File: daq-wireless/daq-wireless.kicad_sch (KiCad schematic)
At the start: 2 parts

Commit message: Easter eggs
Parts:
- added J3: USB_C_Receptacle_USB2.0, symbol Connector:USB_C_Receptacle_USB2.0
- added J4: 5223002-2, !footprints:52230042, symbol semiactive-altium-import:0_mirrored_5223002-2
- added R2, R3: 5.1k, symbol Device:R
- J2: renamed from J?; footprint (none) -> Connector_Card:microSD_HC_Hirose_DM3AT-SF-PEJM5
- gave numbers to parts that had none: 1
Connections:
- new net: J3.A1 (GND), J3.A12 (GND), J3.B1 (GND), J3.B12 (GND)
- new net: J3.A4 (VBUS), J3.A9 (VBUS), J3.B4 (VBUS), J3.B9 (VBUS)
- new net: J3.A5 (CC1), R3.1
- new net: J3.B5 (CC2), R2.1
- new net 3.3V: J4.7, J4.8, J4.9
- new net 5V: J4.4, J4.5, J4.6
- new net 8.4V: J4.1, J4.2, J4.3
- new net CAN_H: J4.20
- new net CAN_L: J4.21
- new net CIPO: J4.17
- new net COPI: J4.18
- new net DIG_OUT: J4.24
- new net DIR1: J4.45
- new net DIR2: J4.46
- new net ENGHALL1: J4.26
- new net ENGHALL2: J4.38
- new net FRBPRESS: J4.47
- new net GND: J4.10, J4.11, J4.12, R2.2, R3.2
- new net I2C_CLK: J4.14
- new net I2C_DATA: J4.13
- new net IR_AMP: J4.35
- new net IR_TEENSY: J4.36
- new net N_A: J4.37
- new net PENC_A: J4.49
- new net PENC_B: J4.51
- new net PLDCLK: J4.57
- new net PLDDAT: J4.58
- new net PLOADC1: J4.41
- new net PLOADC2: J4.42
- new net PWM1: J4.43
- new net PWM2: J4.44
- new net RPOT1: J4.22
- new net RPOT2: J4.23
- new net RRBPRESS: J4.48
- new net RRHALL: J4.25
- new net RX: J4.16
- new net SCLK: J4.19
- new net SENC_A: J4.53
- new net SENC_B: J4.55
- new net SLDCLK: J4.59
- new net SLDDAT: J4.60
- new net SLOADC1: J4.39
- new net SLOADC2: J4.40
- new net SPARK: J4.27
- new net TEMP1: J4.28
- new net TEMP2: J4.29
- new net TEMP3: J4.30
- new net TEMP4: J4.31
- new net TX: J4.15
- new net VOLT1: J4.32
- new net VOLT2: J4.33
- new net VOLT3: J4.34
- new net ~PENC_A: J4.50
- new net ~PENC_B: J4.52
- new net ~SENC_A: J4.54
- new net ~SENC_B: J4.56
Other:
- moved on the sheet: J2

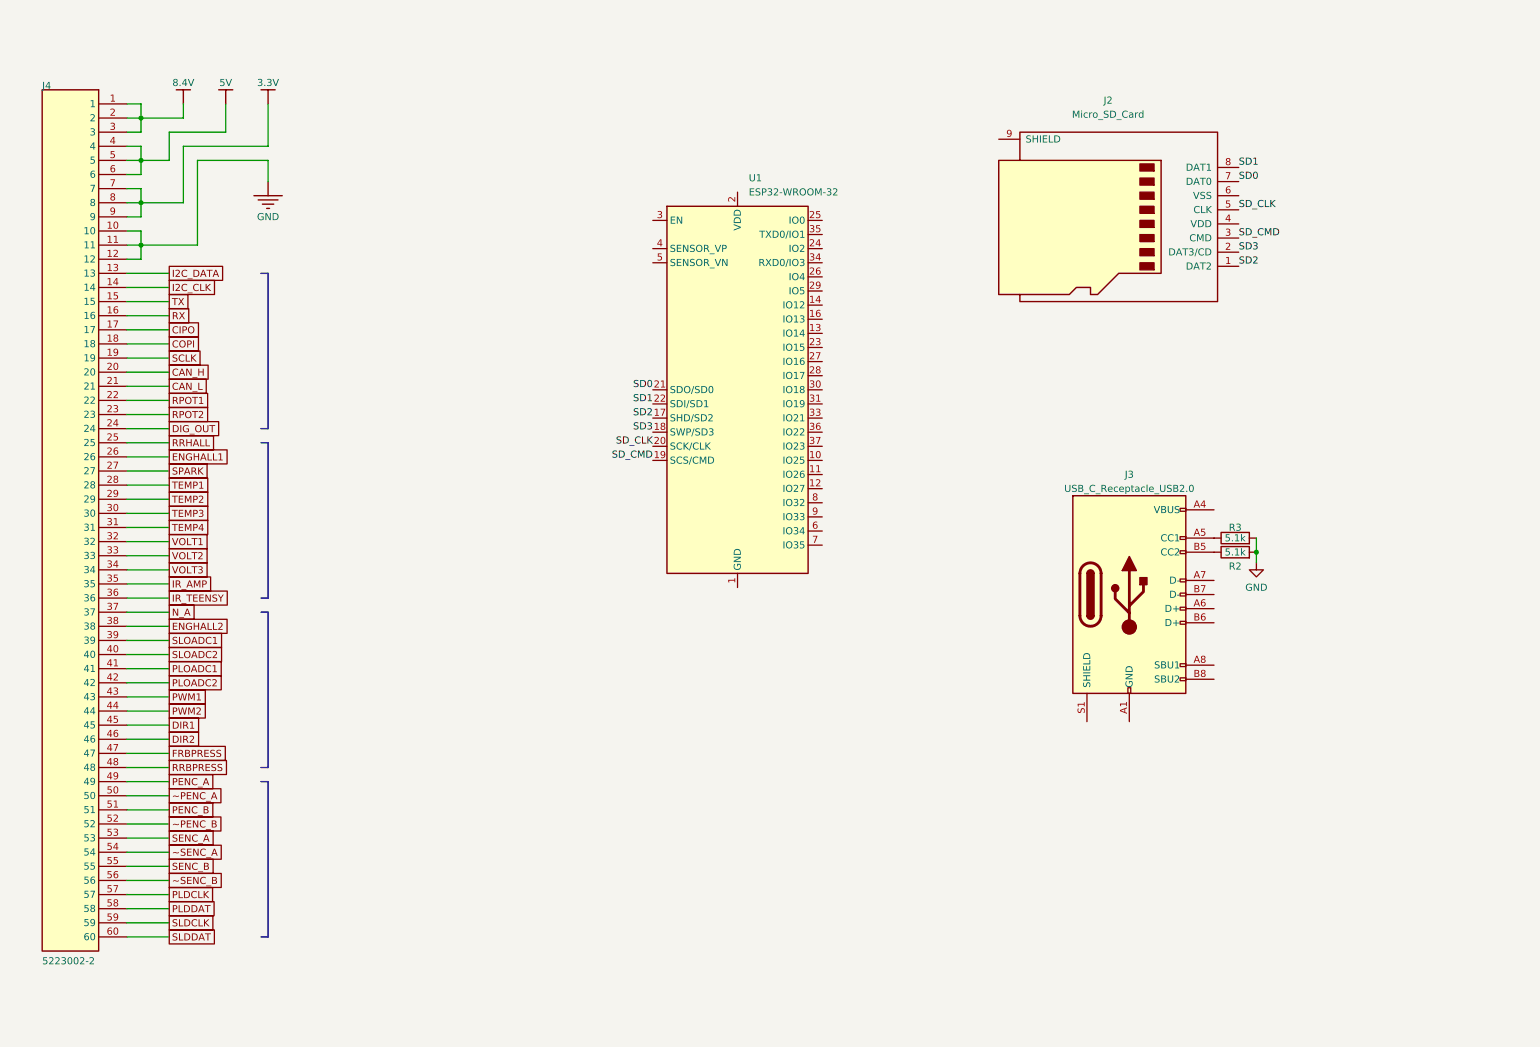
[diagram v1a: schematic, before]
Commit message: Semiactive, DAQ-wireless updates (schem, board)
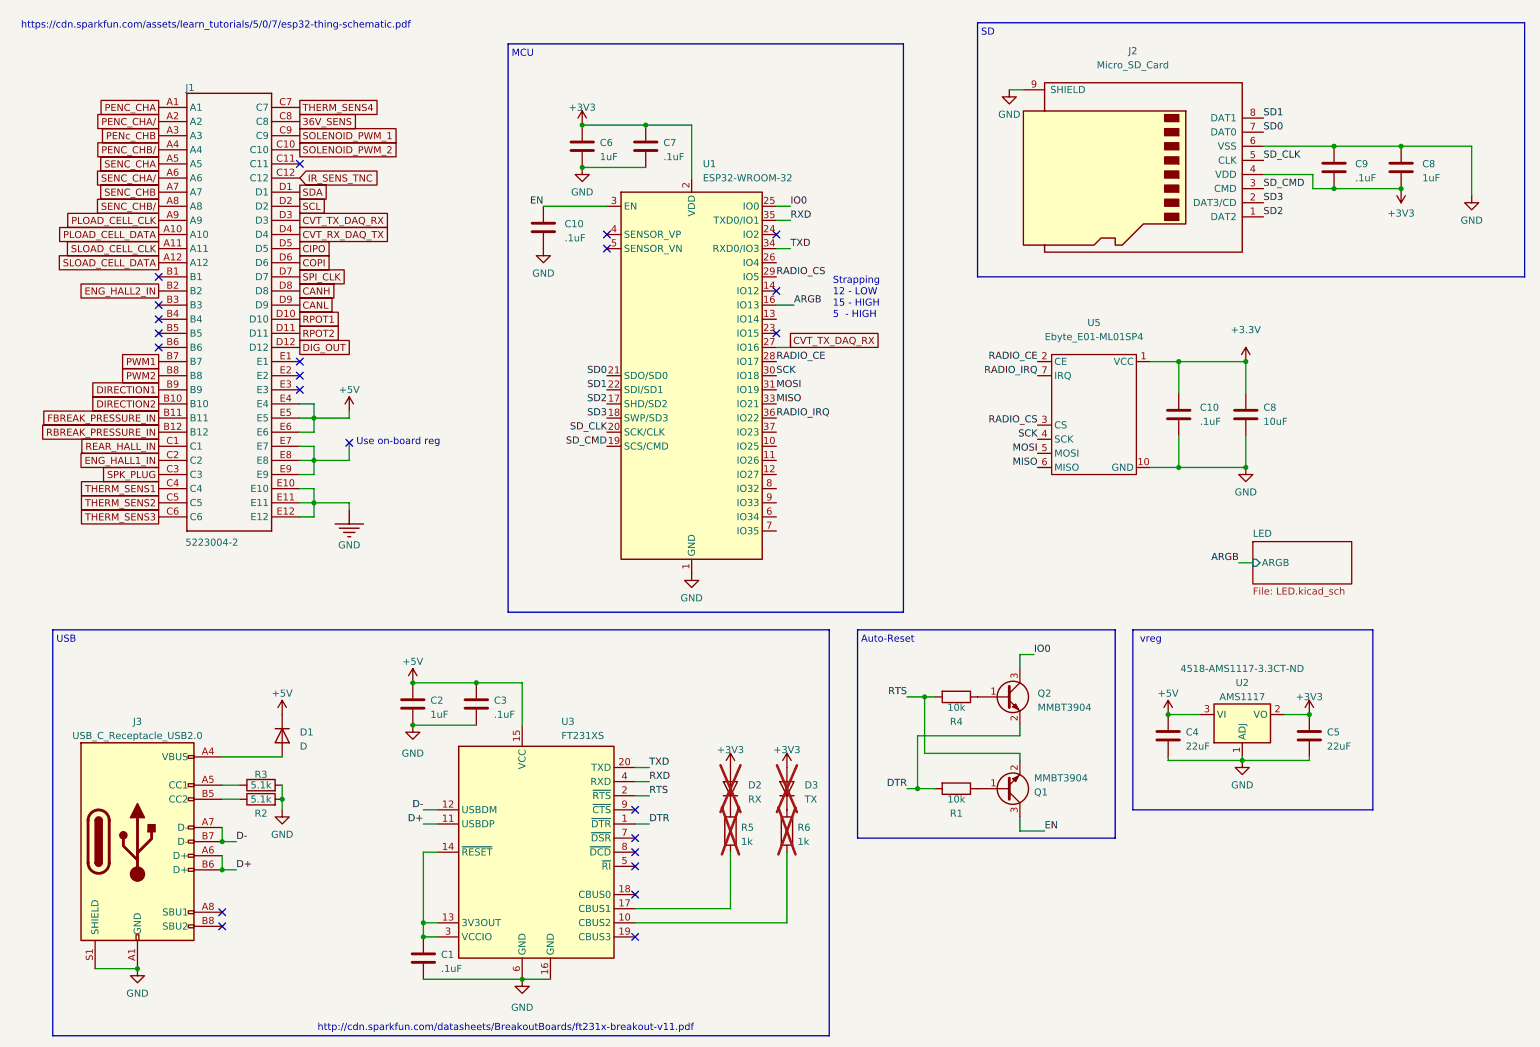
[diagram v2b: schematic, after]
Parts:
- removed J4: 5223002-2, !footprints:52230042, symbol semiactive-altium-import:0_mirrored_5223002-2
- added C1, C10 (x2), C3, C7, C9: .1uF, Capacitor_SMD:C_0402_1005Metric, symbol Device:C
- added C2, C6, C8: 1uF, Capacitor_SMD:C_0603_1608Metric, symbol Device:C
- added C4, C5: 22uF, Capacitor_SMD:C_0805_2012Metric, symbol Device:C
- added C8: 10uF, Capacitor_SMD:C_0603_1608Metric, symbol Device:C
- added D1: D, Diode_SMD:D_SMA, symbol Device:D
- added D2: RX, Diode_SMD:D_0805_2012Metric, symbol Device:D
- added D3: TX, Diode_SMD:D_0805_2012Metric, symbol Device:D
- added J1: 5223004-2, !footprints:52230042, symbol semiactive-altium-import:root_0_5223004-2
- added Q1, Q2: MMBT3904, Package_TO_SOT_SMD:SOT-23, symbol Transistor_BJT:MMBT3904
- added R1, R4: 10k, Resistor_SMD:R_0603_1608Metric, symbol Device:R
- added R5, R6: 1k, Resistor_SMD:R_0603_1608Metric, symbol Device:R
- added U2: AMS1117, Package_TO_SOT_SMD:SOT-223-3_TabPin2, symbol Regulator_Linear:AMS1117
- added U3: FT231XS, Package_SO:SSOP-20_3.9x8.7mm_P0.635mm, symbol Interface_USB:FT231XS
- added U5: Ebyte_E01-ML01SP4, !footprints:Ebyte E01-ML01SP4, symbol CustomParts:Ebyte_E01-ML01SP4
- J2: DPN (none) -> HR1964CT-ND
- J3: footprint (none) -> Connector_USB:USB_C_Receptacle_GCT_USB4105-xx-A_16P_TopMnt_Horizontal; DPN (none) -> 2073-USB4105-GF-ACT-ND
- R2, R3: footprint (none) -> Resistor_SMD:R_0603_1608Metric
- U1: DPN (none) -> 1965-ESP32-WROOM-32E-N8R2CT-ND
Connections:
- net CIPO: now also J1.D5
- net COPI: now also J1.D6
- net DIG_OUT: now also J1.D12
- net GND: now also J2.6 (VSS), J2.9 (SHIELD), J3.A1 (GND), J3.A12 (GND), J3.B1 (GND), J3.B12 (GND), J3.S1 (SHIELD), U1.1 (GND), U1.15 (GND), U1.38 (GND), U1.39 (GND), C1.2, C10.2, C10.2, C2.2, C3.2, C4.2, C5.2, C6.2, C7.2, C8.2, C8.2, C9.2, J1.E10, J1.E11, J1.E12, U2.1 (ADJ), U3.16 (GND), U3.6 (GND), U5.10 (GND), U5.8 (GND), U5.9 (GND)
- net PWM1: now also J1.B7
- net PWM2: now also J1.B8
- net RPOT1: now also J1.D10
- net RPOT2: now also J1.D11
- net ARGB: now reaches U1.16 (IO13)
- net +3V3: now reaches U1.2 (VDD)
- net +3V3: now also J2.4 (VDD), C10.1, C5.1, C6.1, C7.1, C8.1, C8.1, C9.1, D2.2 (A), D3.2 (A), U2.2 (VO), U5.1 (VCC)
- net IO0: now reaches U1.25 (IO0)
- net IO0: now also Q2.3 (C)
- net CVT_TX_DAQ_RX: now reaches U1.27 (IO16)
- net CVT_TX_DAQ_RX: now also J1.D3
- net RADIO_CE: now reaches U1.28 (IO17)
- net RADIO_CE: now also U5.2 (CE)
- net RADIO_CS: now reaches U1.29 (IO5)
- net RADIO_CS: now also U5.3 (CS)
- net EN: now reaches U1.3 (EN)
- net EN: now also C10.1, Q1.3 (C)
- net SCK: now reaches U1.30 (IO18)
- net SCK: now also U5.4 (SCK)
- net MOSI: now reaches U1.31 (IO19)
- net MOSI: now also U5.5 (MOSI)
- net MISO: now reaches U1.33 (IO21)
- net MISO: now also U5.6 (MISO)
- net TXD: now reaches U1.34 (RXD0/IO3)
- net TXD: now also U3.20 (TXD)
- net RXD: now reaches U1.35 (TXD0/IO1)
- net RXD: now also U3.4 (RXD)
- net RADIO_IRQ: now reaches U1.36 (IO22)
- net RADIO_IRQ: now also U5.7 (IRQ)
- net at J3.A4 (VBUS), J3.A9 (VBUS), J3.B4 (VBUS)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: now also D1.2 (A)
- net D+: now reaches J3.A6 (D+)
- net D+: now also J3.B6 (D+), U3.11 (USBDP)
- net D-: now reaches J3.A7 (D-)
- net D-: now also J3.B7 (D-), U3.12 (USBDM)
- new net: D2.1 (K), R5.1
- new net: Q1.1 (B), R1.1
- new net: R5.2, U3.17 (CBUS1)
- new net: C1.1, U3.13 (3V3OUT), U3.14 (~{RESET}), U3.3 (VCCIO)
- new net: R6.2, U3.10 (CBUS2)
- new net: Q2.1 (B), R4.1
- new net: J1.E7, J1.E8, J1.E9
- new net: D3.1 (K), R6.1
- new net +5V: C2.1, C3.1, C4.1, D1.1 (K), J1.E4, J1.E5, J1.E6, U2.3 (VI), U3.15 (VCC)
- new net 36V_SENS: J1.C8
- new net CANH: J1.D8
- new net CANL: J1.D9
- new net CVT_RX_DAQ_TX: J1.D4
- new net DIRECTION1: J1.B9
- new net DIRECTION2: J1.B10
- new net DTR: Q2.2 (E), R1.2, U3.1 (~{DTR})
- new net ENG_HALL1_IN: J1.C2
- new net ENG_HALL2_IN: J1.B2
- new net FBREAK_PRESSURE_IN: J1.B11
- new net IR_SENS_TNC: J1.C12
- new net PENC_CHA: J1.A1
- new net PENC_CHA/: J1.A2
- new net PENC_CHB/: J1.A4
- new net PENc_CHB: J1.A3
- new net PLOAD_CELL_CLK: J1.A9
- new net PLOAD_CELL_DATA: J1.A10
- new net RBREAK_PRESSURE_IN: J1.B12
- new net REAR_HALL_IN: J1.C1
- new net RTS: Q1.2 (E), R4.2, U3.2 (~{RTS})
- new net SCL: J1.D2
- new net SDA: J1.D1
- new net SENC_CHA: J1.A5
- new net SENC_CHA/: J1.A6
- new net SENC_CHB: J1.A7
- new net SENC_CHB/: J1.A8
- new net SLOAD_CELL_CLK: J1.A11
- new net SLOAD_CELL_DATA: J1.A12
- new net SOLENOID_PWM_1: J1.C9
- new net SOLENOID_PWM_2: J1.C10
- new net SPI_CLK: J1.D7
- new net SPK_PLUG: J1.C3
- new net THERM_SENS1: J1.C4
- new net THERM_SENS2: J1.C5
- new net THERM_SENS3: J1.C6
- new net THERM_SENS4: J1.C7
- no-connect marks 0 -> 23
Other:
- added sheet LED (LED.kicad_sch)
- note added: "Auto-Reset"
- note added: "MCU"
- note added: "SD"
- note added: "Strapping 12 - LOW 15 - HIGH 5 - HIGH"
- note added: "USB"
- note added: "Use on-board reg"
- note added: "http://cdn.sparkfun.com/datasheets/BreakoutBoards/ft231x-breakout-v11.pdf"
- note added: "https://cdn.sparkfun.com/assets/learn_tutorials/5/0/7/esp32-thing-schematic.pdf"
- note added: "vreg"
- moved on the sheet: J2, J3, R2, R3, U1

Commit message: DAQ updates
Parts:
- added R7: 10k, Resistor_SMD:R_0603_1608Metric, symbol Device:R
- added SW1: RESET, Button_Switch_THT:SW_PUSH_6mm, symbol Switch:SW_Push
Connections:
- net +3V3: now also R7.1
- net EN: now also R7.2, SW1.2
- net GND: now also SW1.1
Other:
- moved on the sheet: C10, C8, U5

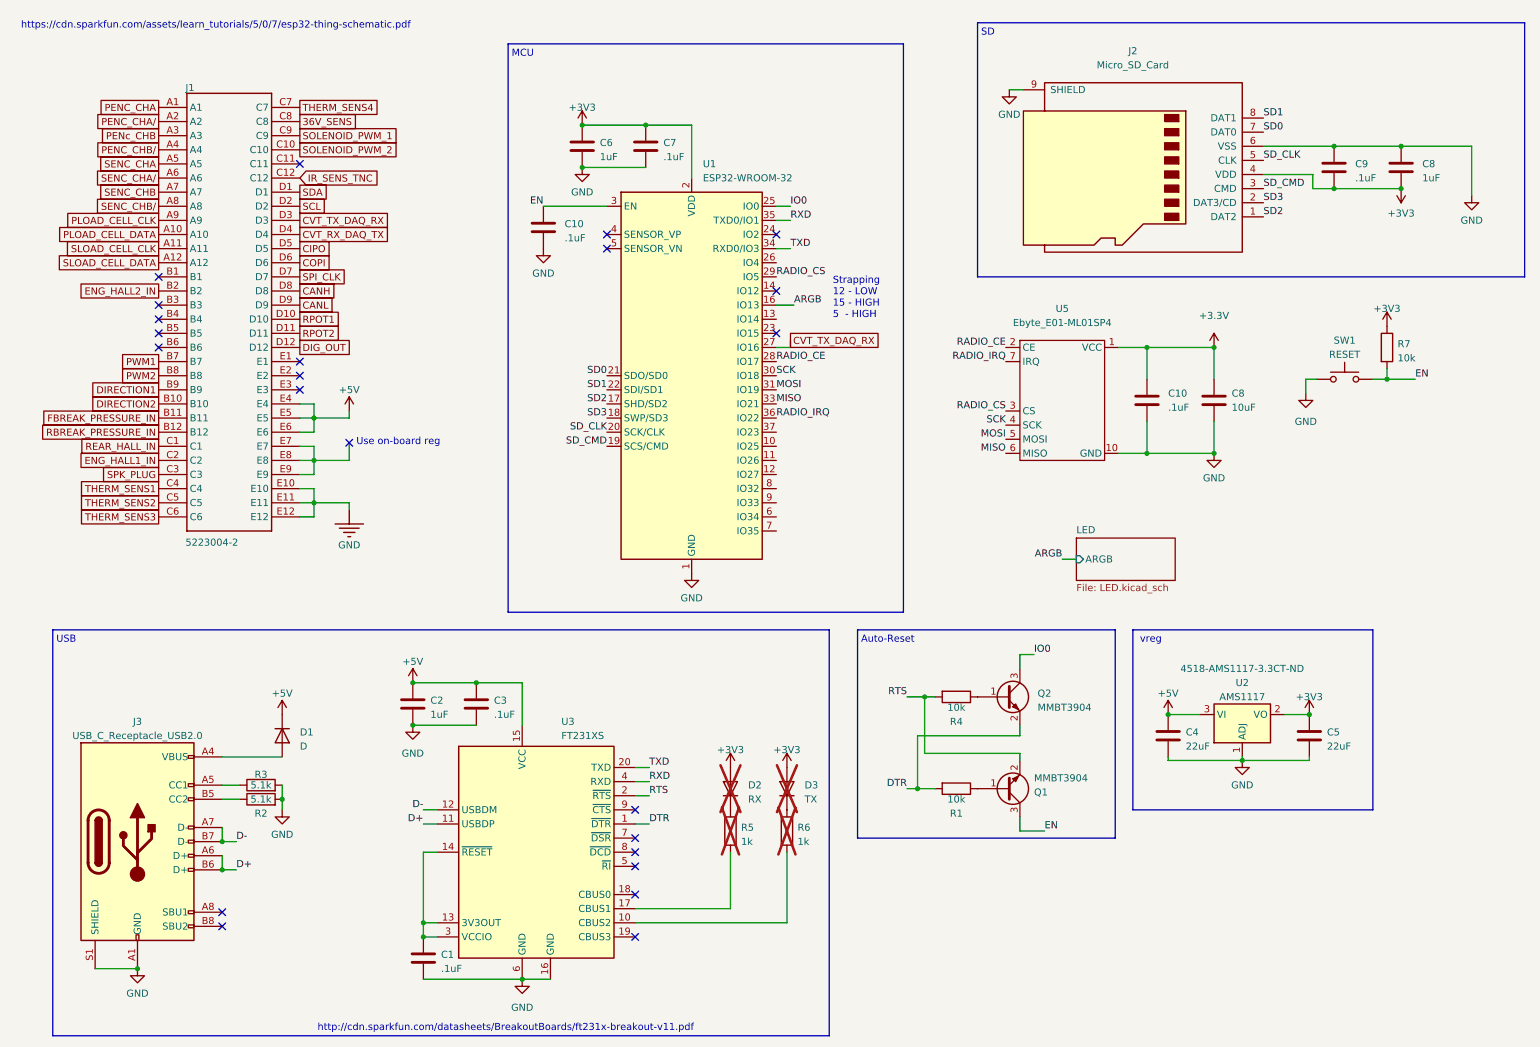
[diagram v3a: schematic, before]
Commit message: Critical ESPdaq fix
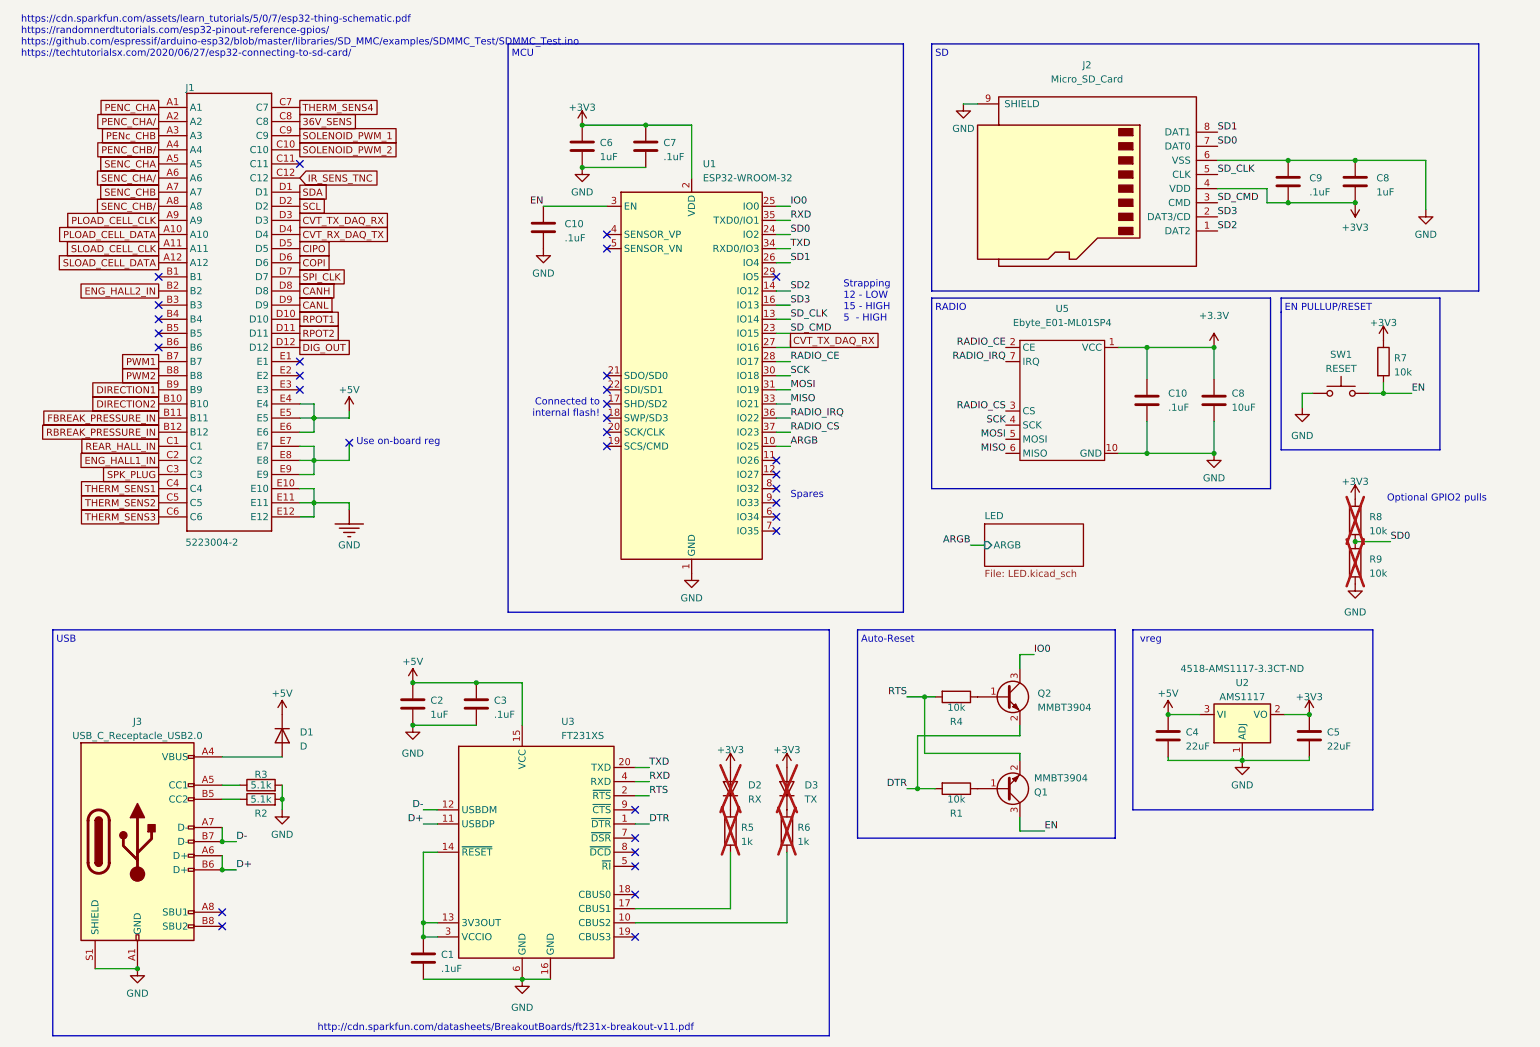
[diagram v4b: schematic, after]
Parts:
- added R8, R9: 10k, Resistor_SMD:R_0603_1608Metric, symbol Device:R
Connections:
- net +3V3: now also R8.1
- net ARGB: now also U1.10 (IO25); no longer U1.16 (IO13)
- net GND: now also R9.2
- net RADIO_CS: now also U1.37 (IO23); no longer U1.29 (IO5)
- net SD0: now also U1.24 (IO2), R8.2, R9.1; no longer U1.21 (SDO/SD0)
- net SD1: now also U1.26 (IO4); no longer U1.22 (SDI/SD1)
- net SD2: now also U1.14 (IO12); no longer U1.17 (SHD/SD2)
- net SD3: now also U1.16 (IO13); no longer U1.18 (SWP/SD3)
- net SD_CLK: now also U1.13 (IO14); no longer U1.20 (SCK/CLK)
- net SD_CMD: now also U1.23 (IO15); no longer U1.19 (SCS/CMD)
- no-connect marks 23 -> 33
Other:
- note added: "Connected to internal flash!"
- note added: "EN PULLUP/RESET"
- note added: "Optional GPIO2 pulls"
- note added: "RADIO"
- note added: "Spares"
- note added: "https://cdn.sparkfun.com/assets/learn_tutorials/5/0/7/esp32-thing-schematic.pdf https://randomnerdtutorials.com/esp32-pinout-reference-gpios/ https://github.com/espressif/arduino-esp32/blob/master/libraries/SD_MMC/examples/SDMMC_Test/SDMMC_Test.ino https://techtutorialsx.com/2020/06/27/esp32-connecting-to-sd-card/"
- note removed: "https://cdn.sparkfun.com/assets/learn_tutorials/5/0/7/esp32-thing-schematic.pdf"
- moved on the sheet: C8, C9, J2, R7, SW1
